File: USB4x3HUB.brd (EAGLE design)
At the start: 79 x 90 mm, 119 parts, among them IC1 TUSB2036, IC10 SN74LVC1G139DCTR, IC2 FSUSB74MPX, IC3 TPS2041C, IC4 TPS2041C, IC5 TPS2041C, IC6 3.3V, IC7 5V, IC8 5V, IC9 5V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

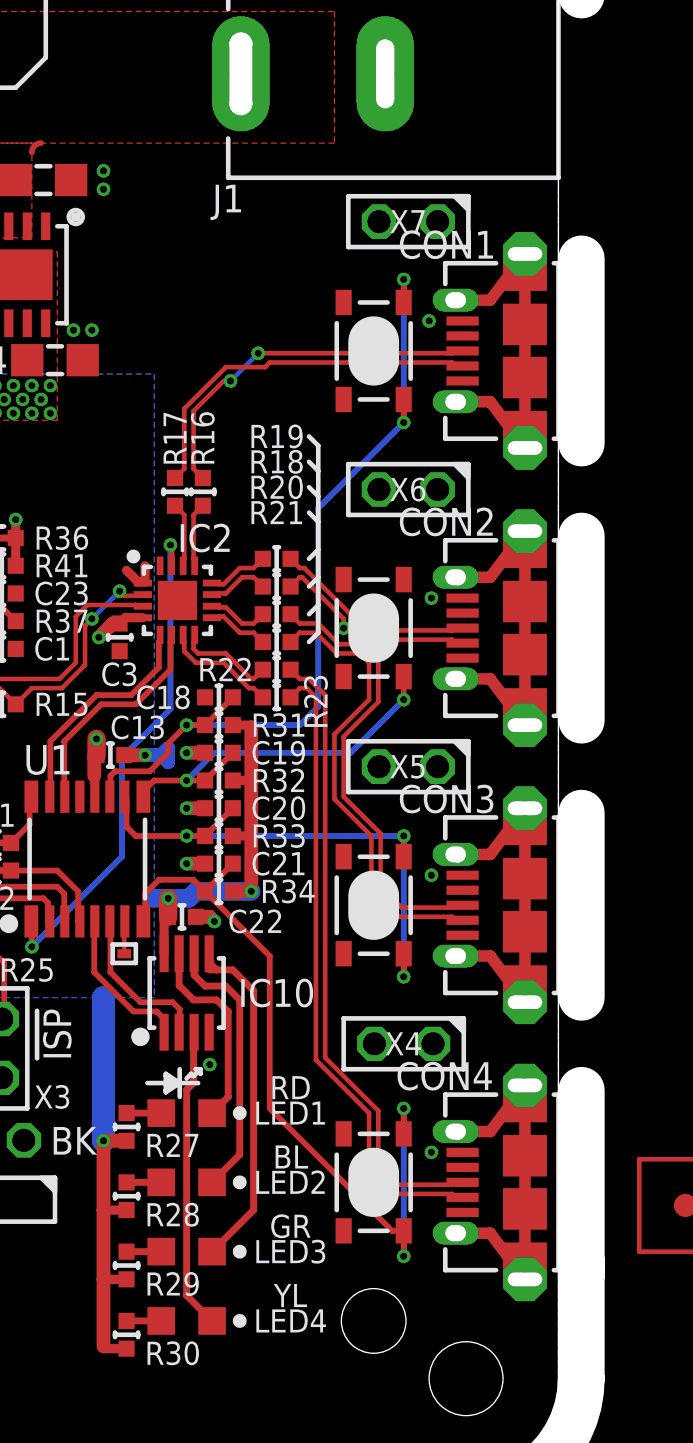
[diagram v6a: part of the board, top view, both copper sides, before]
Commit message: [ BRD ] X4-7 pin1 connects to each switch inputs
- move SW1-4 silk
- move CON1-4 silk
- move X4-7 silk
- add 2.8mm hole for M2.6 screw
   - add tRestrict zone for it
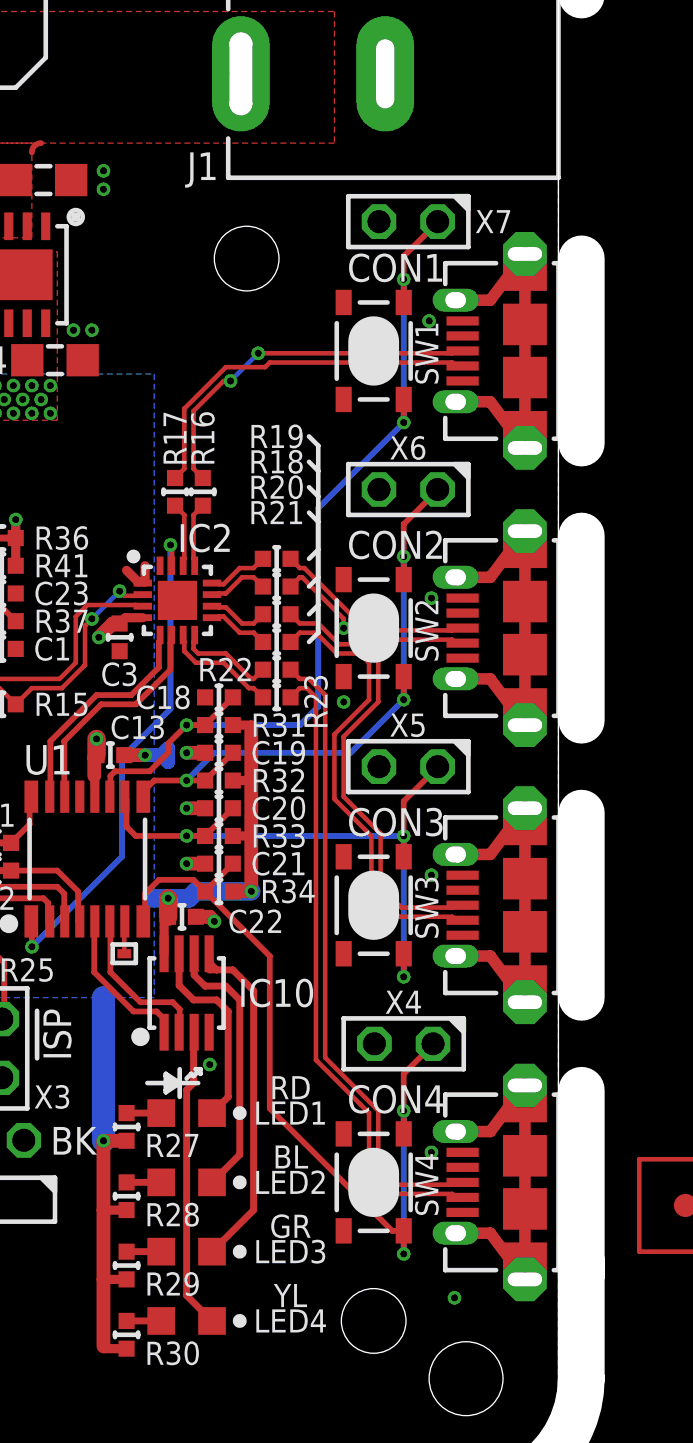
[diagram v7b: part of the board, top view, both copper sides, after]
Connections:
- net GND: now also X4.2, X5.2, X6.2, X7.2
- net SW1: now also X7.1
- net SW2: now also X6.1
- net SW3: now also X5.1
- net SW4: now also X4.1
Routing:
- net SW2: track 16.7 -> 27.4 mm, vias 2 -> 3
- net SW3: track 24.0 -> 27.6 mm
- net SW1: track 35.9 -> 39.1 mm
- net SW4: track 33.2 -> 36.3 mm
- net GND: vias 25 -> 27
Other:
- board text added: "enclosure material t=1.5 +) space=3.95 -> 4.0 +) board t=1.2 ---------------------------- total '=, 6.5"
